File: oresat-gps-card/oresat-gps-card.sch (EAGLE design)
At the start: 353 parts, among them J1 ORESAT-DEBUG-CONNECTOR-CARD, J100 DM3BT-DSF-PEJS, J102 FTSH-105-XX-X-DV-K, J4 TFM-120-01-L-D-RA, Q1 MMBT2907, Q2 PMV45EN, Q3 DMP2240UDM, Q4 PMV45EN, Q5 MOSFET-PCH-SOT23-6, Q6 MOSFET-PCH-SOT23-6, U1 RCLAMP0504FB, U10 TLVH431, U11 TCAN330, U12 MIC842LYC5, U13 MIC842LYC5, U14 MAX4211FETE, U15 TPS62112, U16 MAX7310ATE, U17 25AAXX, U18 VENUS838FLPX-L, U19 BP2G+, U2 TPS2051CDBVR, U20 MAX8510EXK29+T, U21 ALM-GP003, U22 LT1719S6, U4 SN74LVC1G07DCK, U5 MAX2769ETI+, U6 7Q-16.368MBG-T, U7 OSD3358-512M-BSM, U8 MAX8510EXK29+T, U9 MAX8510EXK29+T, Y1 24MHz, Y2 ABS07-32.768KHZ-T

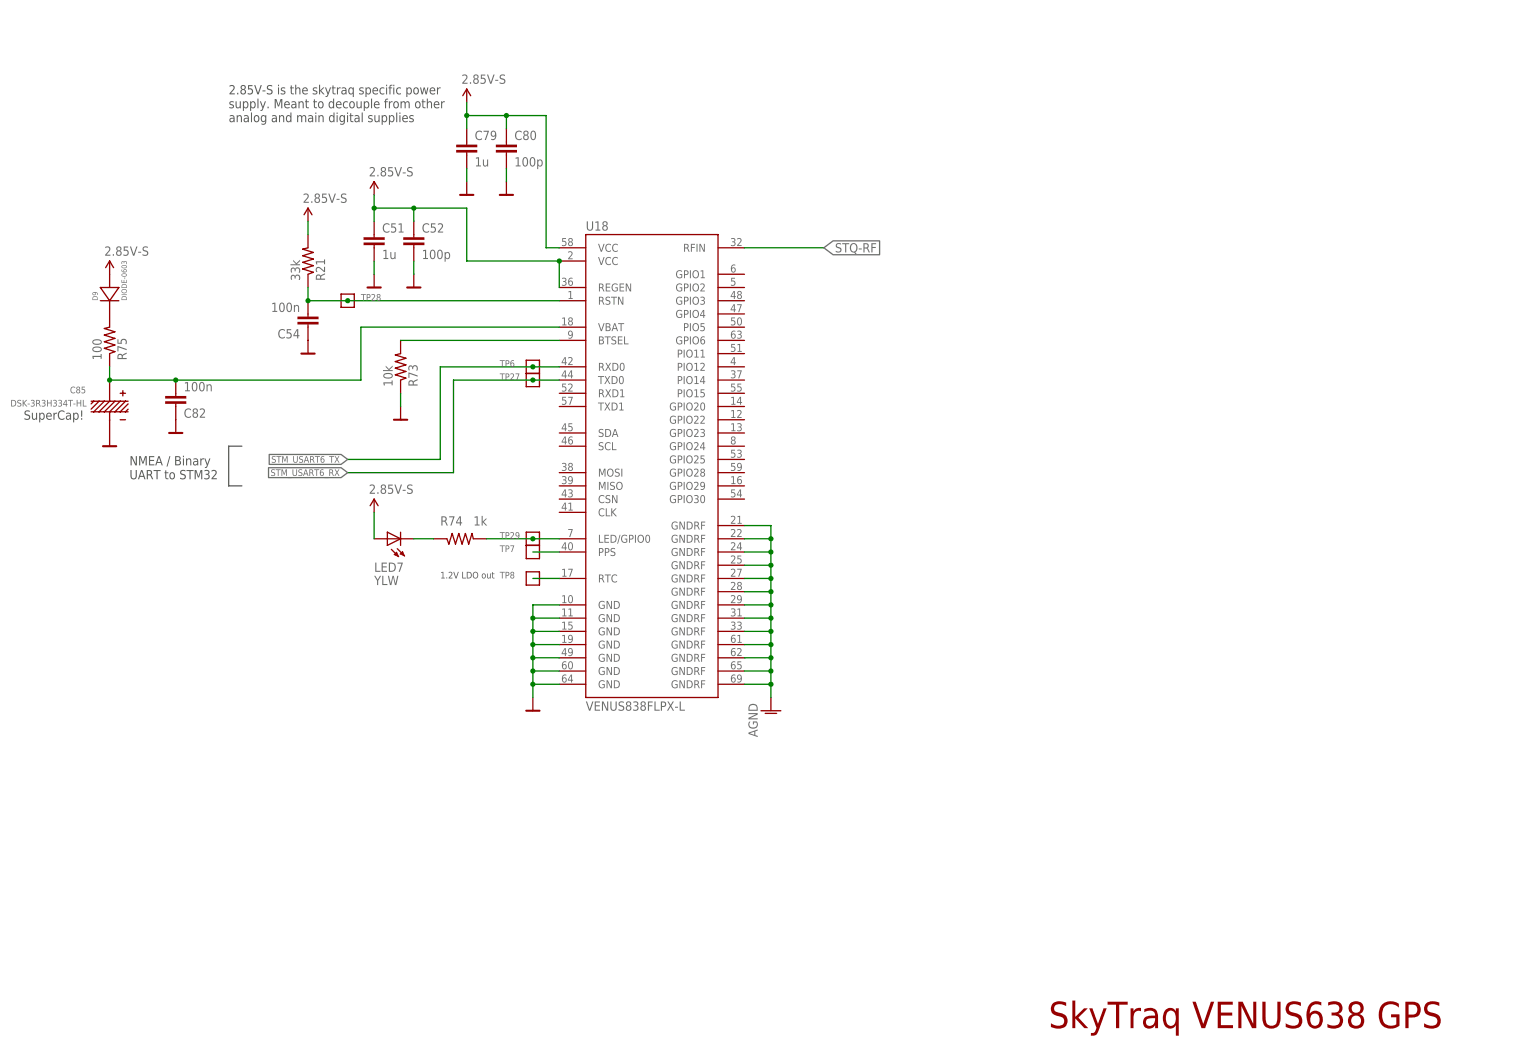
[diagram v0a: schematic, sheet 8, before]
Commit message: GPS card has been mostly layed out. Still missing a few things, but nothing major.
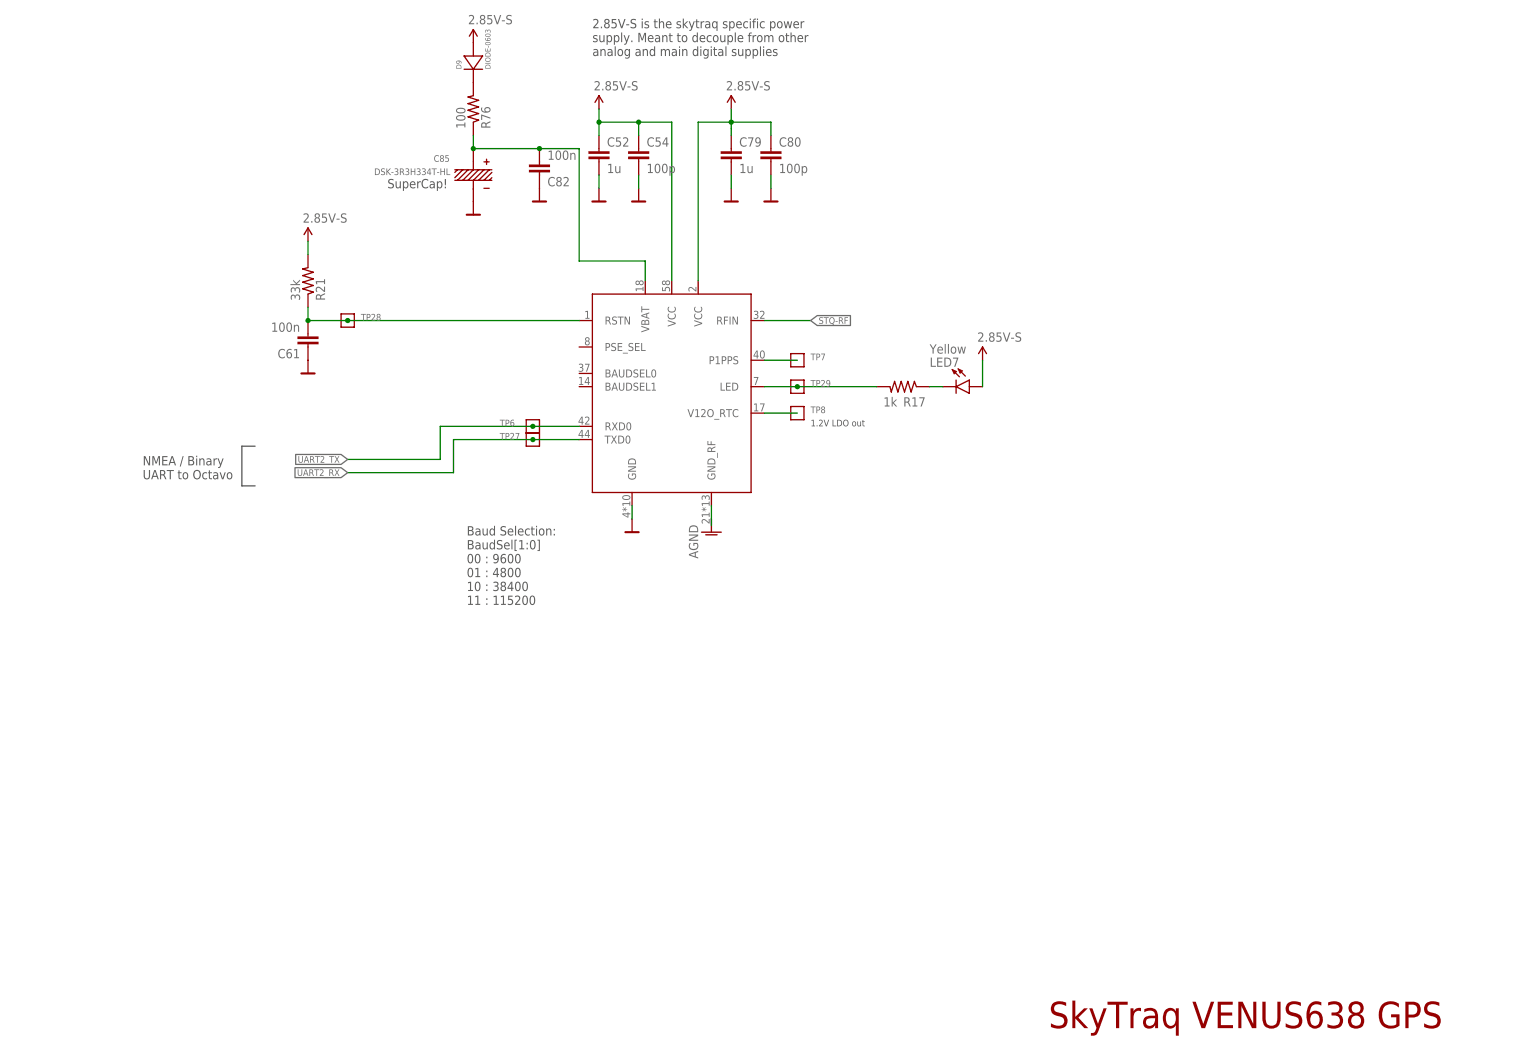
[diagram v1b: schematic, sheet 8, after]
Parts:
- removed JP2: (no value), pinhead:PINHD-1X5
- removed L2: 22n, rcl_custom:L-US0402-B-NOSILK
- removed L5: 1.8n, rcl_custom:L-US0402-B-NOSILK
- removed R14: 1k, rcl_custom:R-US_0402-C-NOSILK
- removed R18: 10, rcl_custom:R-US_0402-C-NOSILK
- removed R29, R30: 4.7k, oresat-rcl:R-US_0603-A
- removed U21: ALM-GP003, ic-lna-ALM-GPxx-Avago:AVAGO-ALM-GPXX
- added CM1: J-MOLEX-SMPM-73300-003X, J-Molex-73300-003X-SMPM-M-edge-mount:J-MOLEX-SMPM-73300-003X
- added L3: 5.6n, oresat-rcl:L-US0402-B-NOSILK
- added R78: 10k, oresat-rcl:R-US_0603-B-NOSILK
- added TP12, TP13, TP16, TP17, TP18, TP19, TP20, TP21, TP23, TP24, TP26, TP32, TP33, TP34, TP36, TP37, TP70: TEST-POINT3X4, SparkFun-Connectors:TEST-POINT3X4
- added U$7: MAX2771ETI+, U-Maxim-MAX2771-Multiband-Universal-GNSS-Receiver:MAX2771ETI+
- added U$8: VENUS838LPX-L, U-Venus-Venus838LPxL-GPS-Module:VENUS838LPX-L
- C16, C17, C20, C21, C23, C24, C25, C26, C27, C28, C42, C43, C55, C56, C57, C60, C69, C70, C80, C82, C83, C84: device rcl_custom:C-EU0402-C-NOSILK -> oresat-rcl:C-EU0603-B-NOSILK
- C41: value 100p -> 0.1uF; device rcl_custom:C-EU0402-C-NOSILK -> oresat-rcl:C-EU0603-A
- C44, C54: value 100n -> 100p; device rcl_custom:C-EU0402-C-NOSILK -> oresat-rcl:C-EU0603-B-NOSILK
- C45: value 10n -> 100n; device rcl_custom:C-EU0402-C-NOSILK -> oresat-rcl:C-EU0603-B-NOSILK
- C46: value 1u -> 10n; device rcl_custom:C-EU0603-B-NOSILK -> oresat-rcl:C-EU0603-B-NOSILK
- C49: value 10n -> 1u; device rcl_custom:C-EU0402-C-NOSILK -> rcl_custom:C-EU0603-B-NOSILK
- C50: value 100n -> 10n; device rcl_custom:C-EU0402-C-NOSILK -> oresat-rcl:C-EU0603-B-NOSILK
- C51: value 1u -> 100n; device rcl_custom:C-EU0603-C-NOSILK -> oresat-rcl:C-EU0603-B-NOSILK
- C52: value 100p -> 1u; device rcl_custom:C-EU0402-C-NOSILK -> oresat-rcl:C-EU0603-B-NOSILK
- C53: device rcl_custom:C-EU0603-B-NOSILK -> oresat-rcl:C-EU0603-B-NOSILK
- C61: value 330p -> 100n; device rcl_custom:C-EU0402-C-NOSILK -> oresat-rcl:C-EU0603-B-NOSILK
- C63: value 100p -> 470p; device rcl_custom:C-EU0402-C-NOSILK -> oresat-rcl:C-EU0402-B-NOSILK
- C64: value 100n -> 1.7p; device rcl_custom:C-EU0402-C-NOSILK -> oresat-rcl:C-EU0402-B-NOSILK
- C79: device rcl_custom:C-EU0603-C-NOSILK -> oresat-rcl:C-EU0603-B-NOSILK
- C81: value 47p -> 56p
- JP107: value JUMPER-SMT_3_NO_NO_SILK -> JUMPER-SMT_3_NO_SILK; device SparkFun-Jumpers:JUMPER-SMT_3_NO_NO_SILK -> SparkFun-Jumpers:JUMPER-SMT_3_NO_SILK
- LED7: value YLW -> Yellow; device led:LEDCHIPLED_0603 -> SparkFun-LED:LED-YELLOW0603
- PCB1: value ORESAT-CARD-V1.2-GENERIC-3XRF-V1.0 -> ORESAT-CARD-V1.3-GENERIC-1RF-POS2; device oresat-cards:ORESAT-CARD-V1.2-GENERIC-3XRF-V1.0 -> oresat-cards:ORESAT-CARD-V1.3-GENERIC-1RF-POS2
- R11, R12, R16, R21: device rcl_custom:R-US_0402-C-NOSILK -> oresat-rcl:R-US_0603-B-NOSILK
- R17: value 10k -> 1k; device rcl_custom:R-US_0402-C-NOSILK -> oresat-rcl:R-US_0603-B-NOSILK
- R73: value 10k -> 100; device rcl_custom:R-US_0402-C-NOSILK -> oresat-rcl:R-US_0603-A
- R74: value 1k -> 100; device rcl_custom:R-US_0402-C-NOSILK -> oresat-rcl:R-US_0603-A
- R75: device rcl_custom:R-US_0402-C-NOSILK -> oresat-rcl:R-US_0603-A
- R76: value 4.7k -> 100; device rcl_custom:R-US_0402-C-NOSILK -> oresat-rcl:R-US_0603-B-NOSILK
- TP10: value TEST-POINT15MIL-TEST-POINT -> TEST-POINT3X4; device Tova:TEST-POINT15MIL-TEST-POINT -> SparkFun-Connectors:TEST-POINT3X4
- U18: value VENUS838FLPX-L -> RCLAMP0504FB; device SparkFun-RF:VENUS638FLPX-L -> U-Semtec-RCLAMP0504FB:RCLAMP0504FB
- U5: value MAX2769ETI+ -> SKY65723-81; device max2769:MAX2769 -> U-Skyworks-SKY65723-81-GPS-LNA-with-filter:SKY65723-81
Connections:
- net SPARE5 renamed N$103
- removed net 3.3VD: C46.1, C47.1, C67.1, C83.1, U20.EN, U20.IN, U22PWR.V+, U8.EN, U8.IN, U9.EN, U9.IN
- removed net ANTBIAS: C63.1, C64.1, TP10.1, U5.ANTBIAS
- removed net D0_I: JP102.1
- removed net D1_I: JP103.1
- removed net D2_I: JP110.1
- removed net D3_I: JP111.1
- removed net LED/GPIO: R74.2, TP29.1, U18.LED/GPIO0
- removed net LNA-POWER-FILTERED: C56.1, C81.1, L2.1, L5.1, R18.2
- removed net MAX_!IDLE: R17.2, U5.!IDLE
- removed net MAX_ANTFLAG: U5.ANTFLAG
- removed net MAX_CFG_!CS: R12.1, U5.!CS
- removed net MAX_CFG_SPI2_MOSI: U5.SDATA
- removed net MAX_CFG_SPI2_SCLK: U5.SCLK
- removed net N$103 (its old number): L5.2, U21.VDD
- removed net N$117 (its old number): C45.1, U6.OUT
- removed net N$118 (its old number): C84.1, R77.1, U22A.-IN
- removed net N$119 (its old number): R73.2, U18.BTSEL
- removed net N$21 (its old number): U21.RF-IN
- removed net N$32 (its old number): C18.1, JP104.1, TP14.1, TP164.1, U4.VCC, U7A.SYS_RTC_1P8V@1, U7A.SYS_RTC_1P8V@2
- removed net N$50 (its old number): TP143.1, U7D.RMII1_REF_CLK
- removed net N$97: TP148.1, U7D.MII1_TX_EN
- removed net PGM: R14.1, U5.PGM
- removed net RTC: TP8.1, U18.RTC
- removed net SCL_2: R30.2, U7C.UART1_RTSN
- removed net SDA_2: R29.2, U7C.UART1_CTSN
- removed net STM_USART6_RX: TP27.1, U18.TXD0
- removed net STM_USART6_TX: TP6.1, U18.RXD0
- new net 3.3VA: C18.1, C41.1, JP104.1, TP14.1, TP164.1, U18.VCC, U4.VCC, U7A.SYS_RTC_1P8V@1, U7A.SYS_RTC_1P8V@2
- new net LED: R17.2, TP29.1, U$8.LED
- new net N$114: R74.2, U7A.I2C0_SDA, U7A.PMIC_SDA
- new net N$115: R75.2, U7A.EEPROM_WP
- new net N$116: R73.2, U7A.I2C0_SCL, U7A.PMIC_SCL
- new net N$123: C63.2, C64.2, L3.1
- new net N$124: L3.2, U$7.LNAIN_HI
- new net N$125: LED7.C, R17.1
- new net N$126: D9.CATHODE, R76.2
- new net N$127: TP8.1, U$8.V12O_RTC
- new net N$129: TP13.1, U7D.MII1_RXD1
- new net N$130: TP16.1, U7D.MII1_RXD2
- new net N$131: TP17.1, U7D.MII1_RXD3
- new net N$133: TP19.1, U7D.MII1_RX_DV
- new net N$15: TP23.1, U7C.MCASP0_AHCLKX
- new net N$16: TP24.1, U7C.MCASP0_AXR1
- new net N$17: TP26.1, U7C.MCASP0_FSR
- new net N$18: TP32.1, U7C.MCASP0_ACLKR
- new net RF-IN: CM1.CENTER, U5.RF_IN
- new net SPI1_CS0: R12.1, TP143.1, U$7.!CSN, U7D.RMII1_REF_CLK
- new net SPI1_D0: TP36.1, U$7.SDATA, U7D.MII1_CRS
- new net SPI1_D1: TP18.1, U7D.MII1_RX_ER
- new net SPI1_SCLK: TP37.1, U$7.SCLK, U7D.MII1_COL
- new net UART2_RX: TP147.1, TP27.1, U$8.TXD0, U7D.MII1_TX_CLK
- new net UART2_TX: TP10.1, TP6.1, U$8.RXD0, U7D.MII1_RX_CLK
- net 2.85V-S: now also C54.1, U$8.VCC@2, U$8.VCC@58; no longer C51.1, U18.REGEN, U18.VCC, U18.VCC@58
- net 2.85VA: now also C45.1, C50.1, C56.1, C81.1, R77.1, U$7.VCCCP, U$7.VCCIF, U$7.VCCRF, U$7.VCCVCO, U5.VCC; no longer C43.1, C48.1, C61.1, L2.2, R18.1, R76.1, U5.VCCCP, U5.VCCIF, U5.VCCRF, U5.VCCVCO
- net 2.85VD: now also C43.1, C51.1, U$7.VCCADC, U$7.VCCD; no longer C41.1, C50.1, U5.VCCADC, U5.VCCD
- net 3.3V: now also C47.1, C48.1, C67.1, C83.1, U20.EN, U20.IN, U22PWR.V+, U8.EN, U8.IN, U9.EN, U9.IN; no longer R29.1, R30.1
- net AGND: now also C45.2, C51.2, C64.1, CM1.SHIELD, CM1.SHIELD1, CM1.SHIELD2, CM1.SHIELD3, U$7.BODY, U$8.GND_RF, U5.GND; no longer C43.2, C50.2, C61.2, C63.2, C64.2, U18.GNDRF@21, U18.GNDRF@22, U18.GNDRF@24, U18.GNDRF@25, U18.GNDRF@27, U18.GNDRF@28, U18.GNDRF@29, U18.GNDRF@31, U18.GNDRF@33, U18.GNDRF@61, U18.GNDRF@62, U18.GNDRF@65, U18.GNDRF@69, U21.GND, U5.BODY
- net CPOUT: now also U$7.CPOUT; no longer U5.CPOUT
- net EEPROM_WP: now also R75.1, U18.I4; no longer U7A.EEPROM_WP
- net GND: now also C43.2, C49.2, C54.2, C61.1, U$8.GND, U18.GND; no longer C46.2, C51.2, C54.1, R14.2, R17.1, R73.1, U18.GND@10, U18.GND@11, U18.GND@15, U18.GND@19, U18.GND@49, U18.GND@60, U18.GND@64
- net I0: now also TP21.1, U$7.I0, U7C.MCASP0_FSX; no longer JP2.4, U5.I0
- net I1: now also TP20.1, U$7.I1, U7C.MCASP0_ACLKX; no longer JP2.5, U5.I1
- net I2C0_SCL: now also R73.1, U18.I2; no longer U7A.I2C0_SCL, U7A.PMIC_SCL
- net I2C0_SDA: now also R74.1, U18.I1; no longer U7A.I2C0_SDA, U7A.PMIC_SDA
- net LNAOUT: now also U$7.LNAOUT_HI; no longer U5.LNAOUT
- net MAX-CLKOUT: now also U7C.XDMA_EVENT_INTR1; no longer JP2.1
- net MAX-RF: now also C63.1, U19.PORT2; no longer U19.PORT1, U5.LNA2
- net MAX_!SHDN: now also TP148.1, U$7.!SHDN, U7D.MII1_TX_EN; no longer U5.!SHDN
- net MAX_CLK_OUT: now also R78.2, U$7.CLKOUT; no longer R77.2, U5.CLKOUT
- net MAX_LD: now also TP70.1, U$7.LD, U7D.MII1_TXD3; no longer U5.LD
- net MIXIN: now also U$7.MIXIN_HI; no longer U5.MIXIN
- net N$113: now also C50.2; no longer C49.2
- net N$120: now also C46.1, U6.OUT; no longer LED7.C, R74.1
- net N$121: now also C84.1, R78.1, U22A.-IN; no longer D9.CATHODE, R75.2
- net N$19: now also U5.RF_OUT; no longer U21.RF-OUT
- net N$24: now also R77.2, U5.VEN; no longer R76.2, U21.SD
- net N$53: now also TP12.1, U7D.MII1_RXD0; no longer TP147.1, U7D.MII1_TX_CLK
- net Q0: now also TP34.1, U$7.Q0, U7C.MCASP0_AHCLKR; no longer JP2.3, U5.Q0
- net Q1: now also TP33.1, U$7.Q1, U7C.MCASP0_AXR0; no longer JP2.2, U5.Q1
- net STQ-!RST: now also C61.2, U$8.RSTN; no longer C54.2, U18.RSTN
- net STQ-PPS: now also U$8.P1PPS; no longer U18.PPS
- net STQ-RF: now also U$8.RFIN, U19.PORT1; no longer U18.RFIN, U19.PORT2
- net STQ-VBAT: now also R76.1, U$8.VBAT; no longer R75.1, U18.VBAT
- net XTAL: now also C46.2, U$7.XTAL; no longer C45.2, U5.XTAL
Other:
- note added: "3.3V Alternate This is used to power a few internal and/or Octavo specific functions, like the power supply clamping circuit, reset circuitry, I2C0 pullup resistors, and the I2C0 ESD protection"
- note added: "Baud Selection: BaudSel[1:0] 00 : 9600 01 : 4800 10 : 38400 11 : 115200"
- note added: "ESD protection clamping diodes for I2C0 lines. This is required because these lines are routed externally so the internal EEPROM can be programmed."
- note added: "GPIO -> PIN map gpio0_28 == mii1_txd0 gpio0_21 == mii1_txd1 gpio0_17 == mii1_txd2 gpio0_16 == mii1_txd3 gpio3_3 == mii1_tx_en gpio3_1 == mii1_crs gpio3_0 == mii1_col gpio2_21 == mii1_rxd0 gpio2_20 == mii1_rxd1 gpio2_19 == mii1_rxd2 gpio2_18 == mii1_rxd3 gpio3_2 == mii1_rx_er gpio3_4 == mii1_rx_dv gpio0_0 == mdio"
- note added: "GPS LNA"
- note added: "MAX Receiver CFG: SPI1_D0 == MII1_CRS SPI1_SCLK == M11_COL SPI1_CS0 == MII1_REF_CLK"
- note added: "NMEA / Binary UART to Octavo"
- note added: "To Skytraq Receiver: UART2 RX == MII1_TX_CLK UART2 TX == MII1_RX_CLK"
- note removed: "GPIO -> PIN map gpio3_9 == mii1_tx_clk gpio0_28 == mii1_txd0 gpio0_21 == mii1_txd1 gpio0_17 == mii1_txd2 gpio0_16 == mii1_txd3 gpio3_3 == mii1_tx_en gpio3_1 == mii1_crs gpio3_0 == mii1_col gpio3_10 == mii1_rx_clk gpio2_21 == mii1_rxd0 gpio2_20 == mii1_rxd1 gpio2_19 == mii1_rxd2 gpio2_18 == mii1_rxd3 gpio3_2 == mii1_rx_er gpio3_4 == mii1_rx_dv gpio0_0 == mdio"
- note removed: "GPS LNA +19 dB, NF = 1.66 dB"
- note removed: "I2C2 SCL == UART1_RTSN == A10 I2C2 SDA == UART1_CTSN == B10"
- note removed: "NMEA / Binary UART to STM32"
- note removed: "Unfortunately MMC0 (SD card) and the PRU share 4 pins. We can get away without using them and just using the 8 highest bits of the camera parallel bus. However, since we will ultimately be booting off of eMMC, we could then utilize the 4 lowest bits. Likewise, populate once only the eMMc is used, cut these jumpers and connect them to the PRUs"
- moved on the sheet: C42, C43, C44, C45, C47, C48, C49, C52, C53, C54, C57, C63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
